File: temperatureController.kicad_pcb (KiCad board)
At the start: 2 copper layers, 86.4 x 61 mm, 23 parts, among them J1 Barrel_Jack, J2 Screw_Terminal_01x02, J3 Conn_01x02_Male, J4 Conn_01x08_Male, Q1 Q_NMOS_GSD, U1 MAX7219

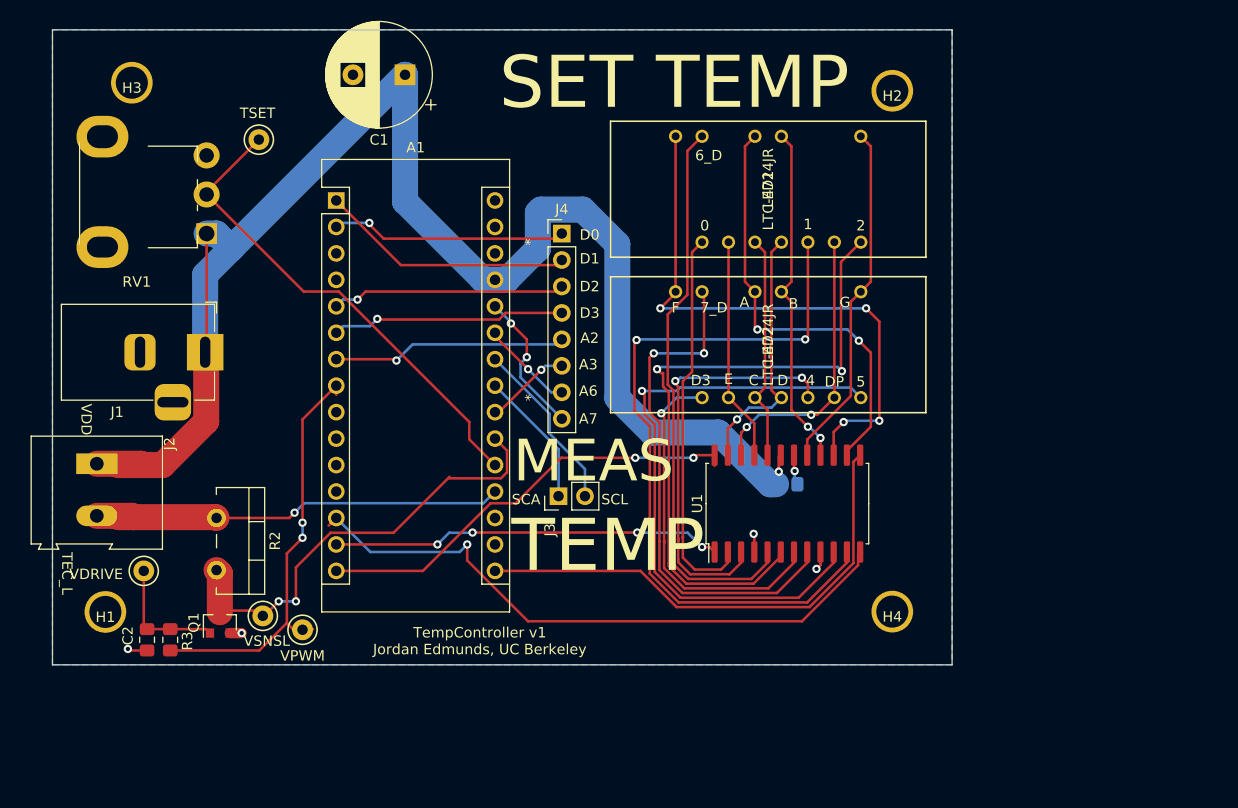
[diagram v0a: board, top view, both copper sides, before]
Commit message: updated PCB to include 60x lower thermal resistance transistor. Added space for heatsink, rearranged some components. Added 6-pin connector for temperature readout
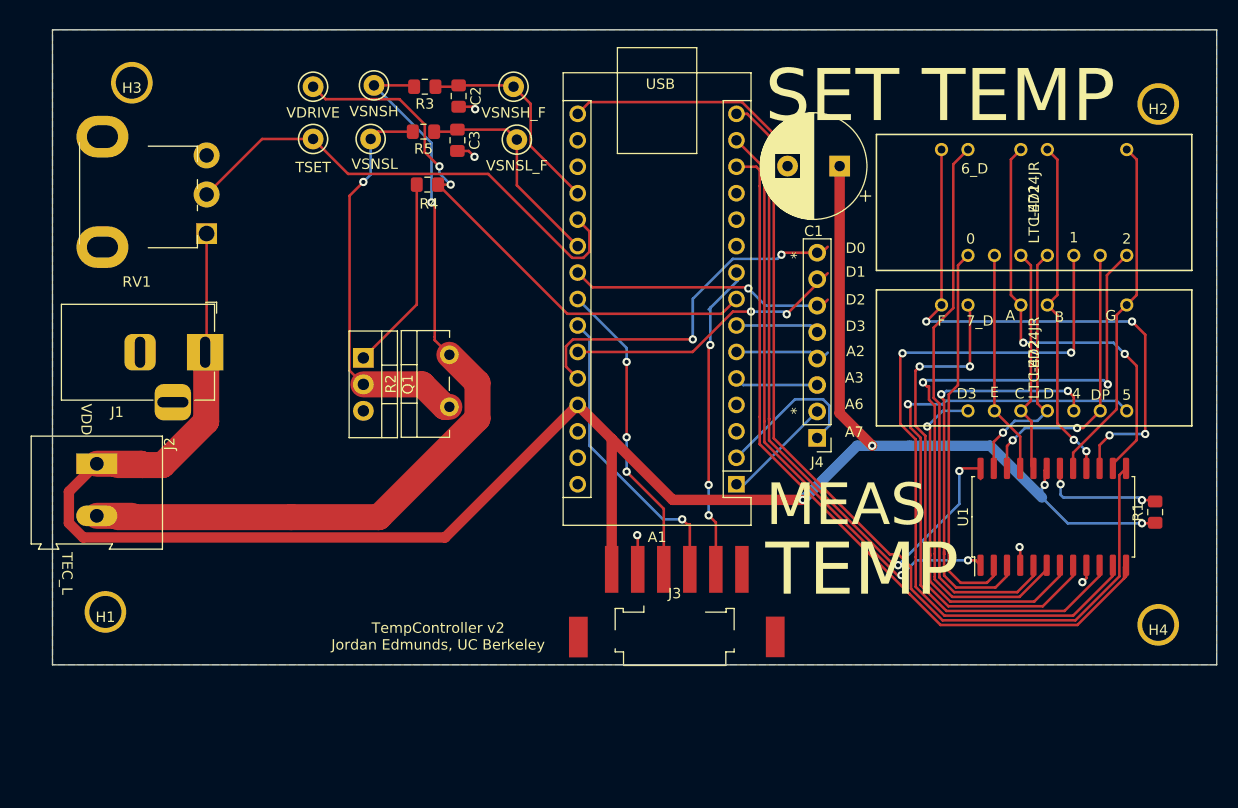
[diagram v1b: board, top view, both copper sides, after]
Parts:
- added C3: C, Capacitor_SMD:C_0805_2012Metric_Pad1.15x1.40mm_HandSolder, F.Cu at (158.3, 67.8)
- added R4: R_US, Resistor_SMD:R_0805_2012Metric_Pad1.15x1.40mm_HandSolder, F.Cu at (155.4, 72.0)
- added R5: R_US, Resistor_SMD:R_0805_2012Metric_Pad1.15x1.40mm_HandSolder, F.Cu at (155.0, 66.9)
- added TP5: VSNSH_F, my_library_foot:TestPoint_Keystone_5000-5004_Miniature, F.Cu at (163.6, 62.6)
- added TP6: VSNSH, my_library_foot:TestPoint_Keystone_5000-5004_Miniature, F.Cu at (150.2, 62.5)
- C2: value 10u -> C
- J3: value Conn_01x02_Male -> Conn_01x06; footprint Connector_PinHeader_2.54mm:PinHeader_1x02_P2.54mm_Vertical -> my_library_foot:S6B-XH-SM4-TB
- Q1: value Q_NMOS_GSD -> Q_NPN_Darlington_BCE; footprint Package_TO_SOT_SMD:SOT-23 -> Package_TO_SOT_THT:TO-220-3_Vertical
- R1: moved to F.Cu
- R3: value 10k -> R_US
- TP2: value VDRIVE -> VSNSL_F
- TP4: value VPWM -> VDRIVE
- moved C2 60.2 mm to (158.4, 63.5)
- moved R3 58.4 mm to (155.1, 62.6), turned to 180 degrees
- moved TP2 54.7 mm to (164.0, 67.7)
- moved TP4 52.1 mm to (144.4, 62.6)
- moved A1 47.1 mm to (185.0, 100.8), turned to 180 degrees
- moved TP1 46.9 mm to (149.9, 67.6)
- moved C1 42.6 mm to (194.9, 70.2)
- moved R1 35.5 mm to (225.2, 103.5), turned to 90 degrees
- moved J4 31.4 mm to (192.8, 96.3), turned to 180 degrees
- moved Q1 28.9 mm to (149.2, 88.6), turned to 270 degrees
- moved LED1 25.6 mm to (207.3, 78.8)
- moved LED2 25.6 mm to (207.3, 93.7)
- moved H2 25.6 mm to (225.5, 64.3)
- moved H4 25.6 mm to (225.5, 114.3)
- moved U1 25.6 mm to (215.5, 103.9)
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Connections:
- A1 pad 19: /TEC_L -> /VSNSH_F
- A1 pad 21: /VSNSL -> /VSNSL_F
- A1 pad 8: /VPWM -> /VDRIVE
- A1 pad 9: Net-(A1-Pad9) -> /ALT
- C2 pad 1: /VDRIVE -> /VSNSH_F
- J2 pad 2: /TEC_L -> /VSNSH
- J3 pad 1: /SDA -> VDD
- J3 pad 2: /SCL -> GND
- Q1 pad 1: /VDRIVE -> Net-(Q1-Pad1)
- Q1 pad 2: GND -> /VSNSL
- Q1 pad 3: /VSNSL -> GND
- R2 pad 1: /TEC_L -> /VSNSL
- R2 pad 2: /VSNSL -> /VSNSH
- R3 pad 1: /VPWM -> /VSNSH_F
- R3 pad 2: /VDRIVE -> /VSNSH
- TP2 pad 1: /VDRIVE -> /VSNSL_F
- TP4 pad 1: /VPWM -> /VDRIVE
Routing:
- net /VSNSH: track 0.00 -> 81.8 mm, vias 0 -> 1
- net /SCK: track 48.2 -> 103.8 mm
- net VDD: track 148.6 -> 202.4 mm, vias 1 -> 4
- net /VDRIVE: track 11.9 -> 54.6 mm, vias 0 -> 2
- net /TEC_L: track 40.8 -> 0.00 mm, vias 1 -> 0
- net /VPWM: track 40.8 -> 0.00 mm, vias 2 -> 0
- net /ALT: track 0.00 -> 30.3 mm, vias 0 -> 3
- net /MISO: track 41.9 -> 65.4 mm
- net /VSNSL_F: track 0.00 -> 21.1 mm
- net /A7: track 14.0 -> 34.5 mm
- net /VSNSH_F: track 0.00 -> 20.4 mm
- net /MOSI: track 37.6 -> 57.3 mm, vias 4 -> 2
- net Net-(Q1-Pad1): track 0.00 -> 18.8 mm
- net /A6: track 8.97 -> 27.2 mm, vias 1 -> 2
- net /A3: track 8.25 -> 25.0 mm
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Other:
- board size 86.4 x 61 mm -> 111.8 x 61 mm
- board text added: "TempController v2 Jordan Edmunds, UC Berkeley"
- board text removed: "SCA"
- board text removed: "SCL"
- board text removed: "TempController v1 Jordan Edmunds, UC Berkeley"

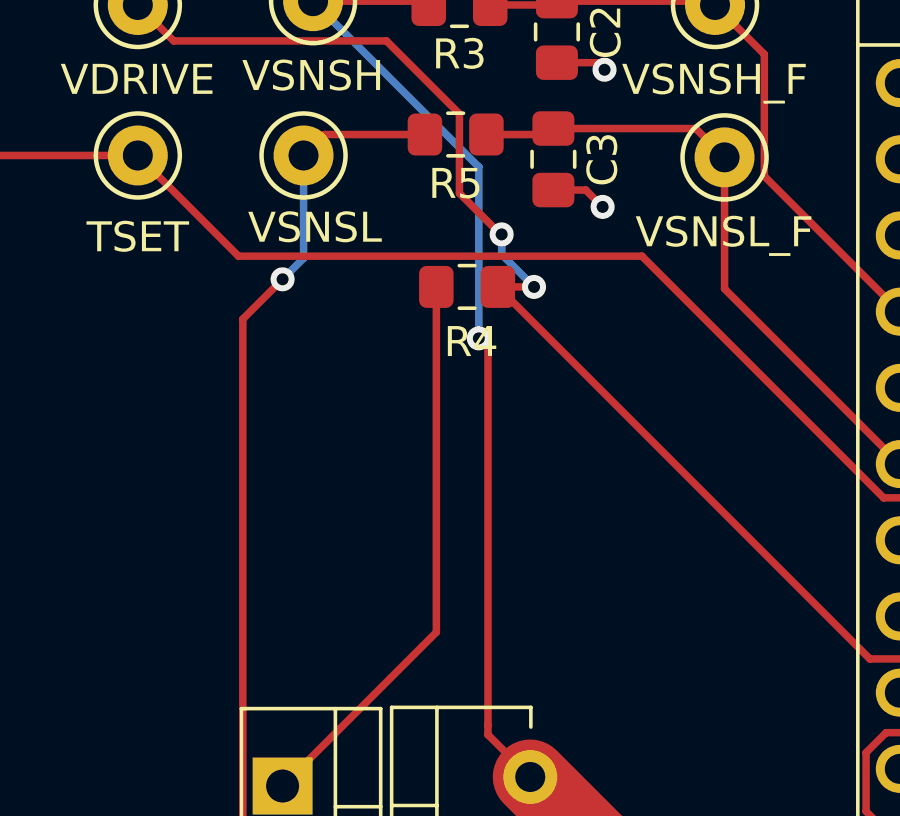
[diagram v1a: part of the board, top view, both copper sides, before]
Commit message: added debugging information to README. Implemented closed-loop temperature control, tuned PI controller to have 30% overshoot and decent transient response. optimal choice of Ti might be slightly longer, should consider changing to PID. Made some minor schematic changes. PCB is tetsed and working well from 1C to 80C.
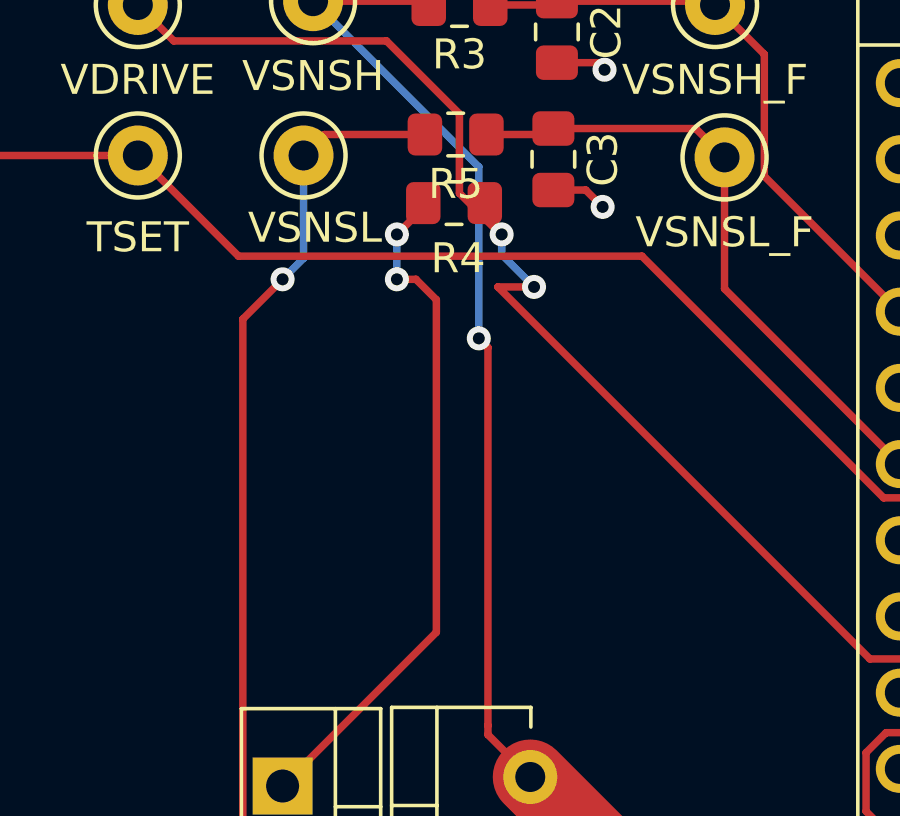
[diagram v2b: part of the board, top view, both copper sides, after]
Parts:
- moved R4 2.83 mm to (154.9, 69.2)
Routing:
- net Net-(Q1-Pad1): track 18.8 -> 22.8 mm, vias 0 -> 2

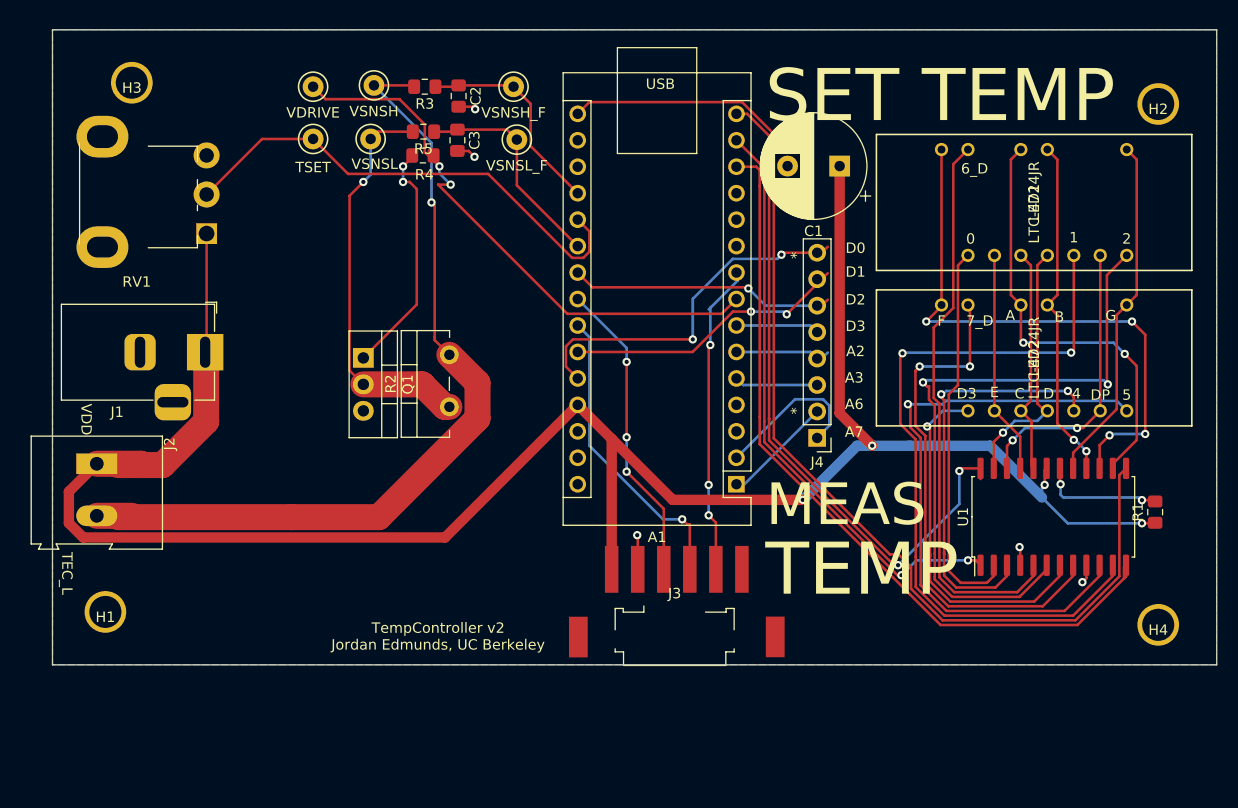
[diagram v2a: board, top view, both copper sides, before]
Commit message: updated PCB with a relay, signal conditioning for sense resistor output. Ready to fabricate
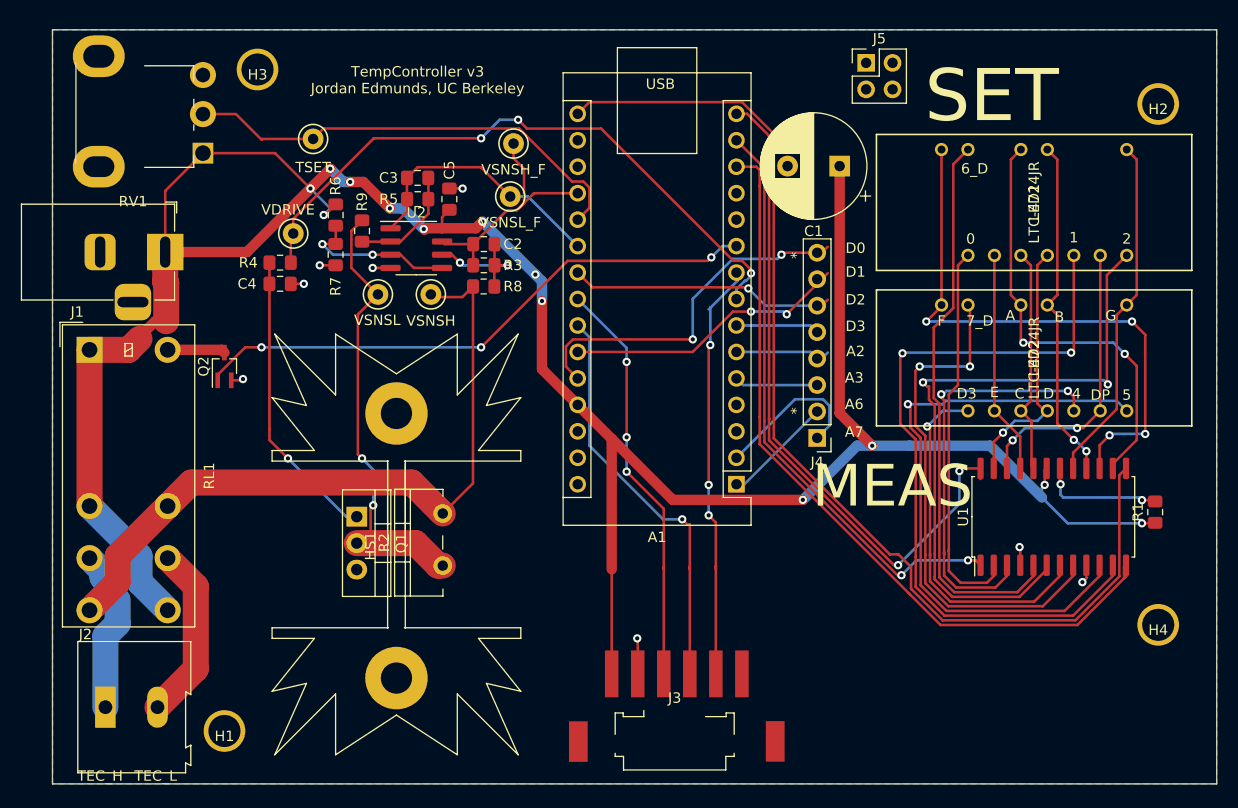
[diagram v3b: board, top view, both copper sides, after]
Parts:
- added C4: 10uF, Capacitor_SMD:C_0805_2012Metric_Pad1.15x1.40mm_HandSolder, F.Cu at (141.2, 81.5)
- added C5: 100nF, Capacitor_SMD:C_0805_2012Metric_Pad1.15x1.40mm_HandSolder, F.Cu at (157.5, 73.4)
- added HS1: Heatsink_Pad, my_library_foot:heatsink, F.Cu at (152.4, 106.7)
- added J5: Conn_02x02_Odd_Even, Connector_PinHeader_2.54mm:PinHeader_2x02_P2.54mm_Vertical, F.Cu at (197.5, 60.3)
- added Q2: Q_NMOS_GSD, Package_TO_SOT_SMD:SOT-323_SC-70_Handsoldering, F.Cu at (135.9, 89.5)
- added R6: 30k, Resistor_SMD:R_0805_2012Metric_Pad1.15x1.40mm_HandSolder, F.Cu at (146.6, 74.9)
- added R7: 10k, Resistor_SMD:R_0805_2012Metric_Pad1.15x1.40mm_HandSolder, F.Cu at (146.6, 78.7)
- added R8: 10k, Resistor_SMD:R_0805_2012Metric_Pad1.15x1.40mm_HandSolder, F.Cu at (160.8, 81.8)
- added R9: 10k, Resistor_SMD:R_0805_2012Metric_Pad1.15x1.40mm_HandSolder, F.Cu at (149.1, 76.5)
- added RL1: G2RL-2-DC5, Relay_THT:Relay_DPDT_Omron_G2RL, F.Cu at (122.9, 87.9)
- added U2: MCP6L02x-xSN, Package_SO:SOIC-8_3.9x4.9mm_P1.27mm, F.Cu at (154.3, 78.1)
- C1: value C -> 100nF
- C2, C3: value C -> 10uF
- R1: value 30k -> 10k
- R3, R5: value R_US -> 10k
- R4: value R_US -> 1k
- moved J2 23.4 mm to (124.5, 122.2), turned to 0 degrees
- moved TP6 20.8 mm to (155.7, 82.5)
- moved R3 18.1 mm to (160.8, 79.8), turned to 0 degrees
- moved R4 17.1 mm to (141.2, 79.5)
- moved H1 16.2 mm to (135.9, 124.5)
- moved Q1 15.3 mm to (148.6, 103.9)
- moved R2 15.3 mm to (156.8, 109.8)
- moved TP1 14.9 mm to (150.6, 82.5)
- moved C2 14.4 mm to (160.8, 77.7), turned to 180 degrees
- moved TP4 14.2 mm to (142.5, 76.7)
- moved H3 12.1 mm to (139.1, 61.0)
- moved J1 10.4 mm to (130.2, 78.5)
- moved J3 10.0 mm to (169.9, 125.5)
- moved RV1 7.73 mm to (133.8, 69.0)
- moved R5 6.50 mm to (154.4, 73.4), turned to 0 degrees
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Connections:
- net Net-(Q1-Pad1) renamed /VDR_F
- A1 pad 10: Net-(A1-Pad10) -> /RELAY
- C2 pad 1: /VSNSH_F -> /VSNSH-
- C2 pad 2: GND -> /VSNSH_F
- C3 pad 2: GND -> /VSNSL-
- J2 pad 1: VDD -> /TECH
- J2 pad 2: /VSNSH -> /TECL
- R3 pad 2: /VSNSH -> /VSNSH-
- R5 pad 2: /VSNSL -> /VSNSL-
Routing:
- net /RELAY: track 0.00 -> 55.4 mm, vias 0 -> 3
- net VDD: track 202.4 -> 254.4 mm, vias 4 -> 13
- net /TECH: track 0.00 -> 26.2 mm
- net /TECL: track 0.00 -> 16.9 mm
- net /VBIAS: track 0.00 -> 15.7 mm, vias 0 -> 2
- net /VSNSH: track 81.8 -> 69.2 mm, vias 1 -> 0
- net /VSNSH-: track 0.00 -> 12.4 mm, vias 0 -> 2
- net /VSNSL-: track 0.00 -> 10.9 mm
- net /ALT: track 30.3 -> 40.7 mm
- net /SCL: track 29.1 -> 39.4 mm
- net /SDA: track 29.4 -> 39.6 mm
- net /VDRIVE: track 54.6 -> 61.6 mm, vias 2 -> 3
- net /VDR_F: track 22.8 -> 28.5 mm, vias 2 -> 1
- net Net-(Q2-Pad3): track 0.00 -> 5.57 mm
- net /VSNSL: track 43.9 -> 48.9 mm, vias 1 -> 2
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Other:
- board size 111.8 x 61 mm -> 111.8 x 72.4 mm
- board text added: "SET"
- board text added: "TEC_H"
- board text added: "TempController v3 Jordan Edmunds, UC Berkeley"
- board text removed: "SET TEMP"
- board text removed: "TEMP"
- board text removed: "TempController v2 Jordan Edmunds, UC Berkeley"
- board text removed: "VDD"

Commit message: updated README, bill of materials with new components and capabilities. Fixed PCB to have a differential amplifier to properly bias the nano's ADC.
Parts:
- R6: value 30k -> 10k
- TP2: value VSNSL_F -> VDD/2
- moved R5 11.1 mm to (147.2, 81.8), turned to 180 degrees
- moved C3 11.1 mm to (147.2, 79.8), turned to 180 degrees
- moved TP2 10.2 mm to (153.5, 70.1)
- moved R9 7.61 mm to (147.2, 83.8), turned to 180 degrees
- moved TP1 5.84 mm to (156.5, 82.5)
- moved R7 3.10 mm to (147.2, 75.7), turned to 180 degrees
- moved TP6 3.05 mm to (152.7, 82.5)
- moved R6 2.86 mm to (147.2, 77.7), turned to 0 degrees
- moved TP4 1.02 mm to (141.5, 76.7)
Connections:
- net /VSNSH_F renamed /VSNS_F
- A1 pad 21: /VSNSL_F -> Net-(A1-Pad21)
- C2 pad 1: /VSNSH- -> /VSNSL-
- C3 pad 1: /VSNSL_F -> /VSNSH+
- C3 pad 2: /VSNSL- -> /2.5V_BUF
- R3 pad 2: /VSNSH- -> /VSNSL-
- R5 pad 1: /VSNSL_F -> /VSNSH+
- R5 pad 2: /VSNSL- -> /2.5V_BUF
- R6 pad 2: /VBIAS -> /2.5V
- R7 pad 1: /VBIAS -> /2.5V
- R8 pad 1: /VSNSH- -> /VSNSL-
- R8 pad 2: /VSNSH -> /VSNSL
- R9 pad 1: /VSNSL- -> /VSNSH+
- R9 pad 2: /VSNSL -> /VSNSH
- TP2 pad 1: /VSNSL_F -> /2.5V_BUF
- U2 pad 1: /VSNSL_F -> /2.5V_BUF
- U2 pad 2: /VSNSL- -> /2.5V_BUF
- U2 pad 3: /VBIAS -> /2.5V
- U2 pad 5: /VBIAS -> /VSNSH+
- U2 pad 6: /VSNSH- -> /VSNSL-
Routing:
- net /VSNSL_F: track 25.5 -> 0.00 mm
- net /2.5V_BUF: track 0.00 -> 21.5 mm, vias 0 -> 2
- net /VBIAS: track 15.7 -> 0.00 mm, vias 2 -> 0
- net /VSNSH+: track 0.00 -> 13.6 mm
- net /VSNSH-: track 12.4 -> 0.00 mm, vias 2 -> 0
- net Net-(A1-Pad21): track 0.00 -> 8.45 mm
- net VDD: track 254.4 -> 246.6 mm, vias 13 -> 11
- net /2.5V: track 0.00 -> 6.07 mm
- net /VSNSH: track 69.2 -> 72.9 mm
- net /VDRIVE: track 61.6 -> 64.7 mm
- net /VSNSL-: track 10.9 -> 12.4 mm, vias 0 -> 2
- net /VSNSL: track 48.9 -> 49.2 mm, vias 2 -> 0
